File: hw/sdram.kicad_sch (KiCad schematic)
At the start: 23 parts, among them U1002 T20Q144xx, U1004 NDS36PT5-16ET

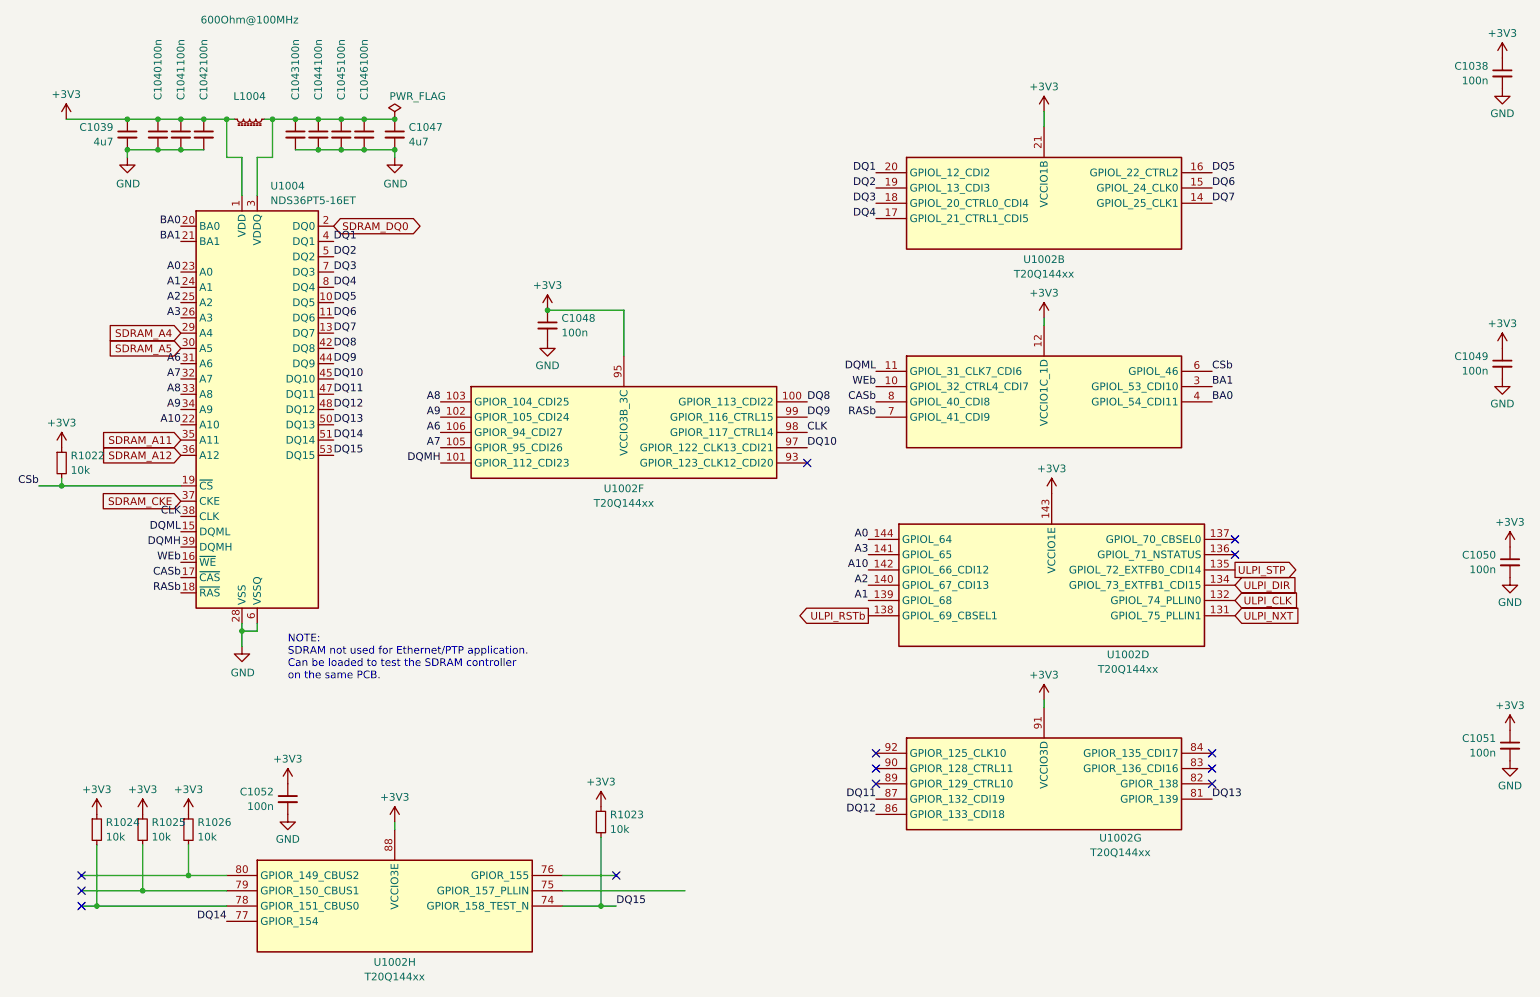
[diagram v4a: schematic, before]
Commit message: layout almost complete with UPLI on the RHS => NO CLOCK INPUT
Have to rework and move the usb transceiver to the left...
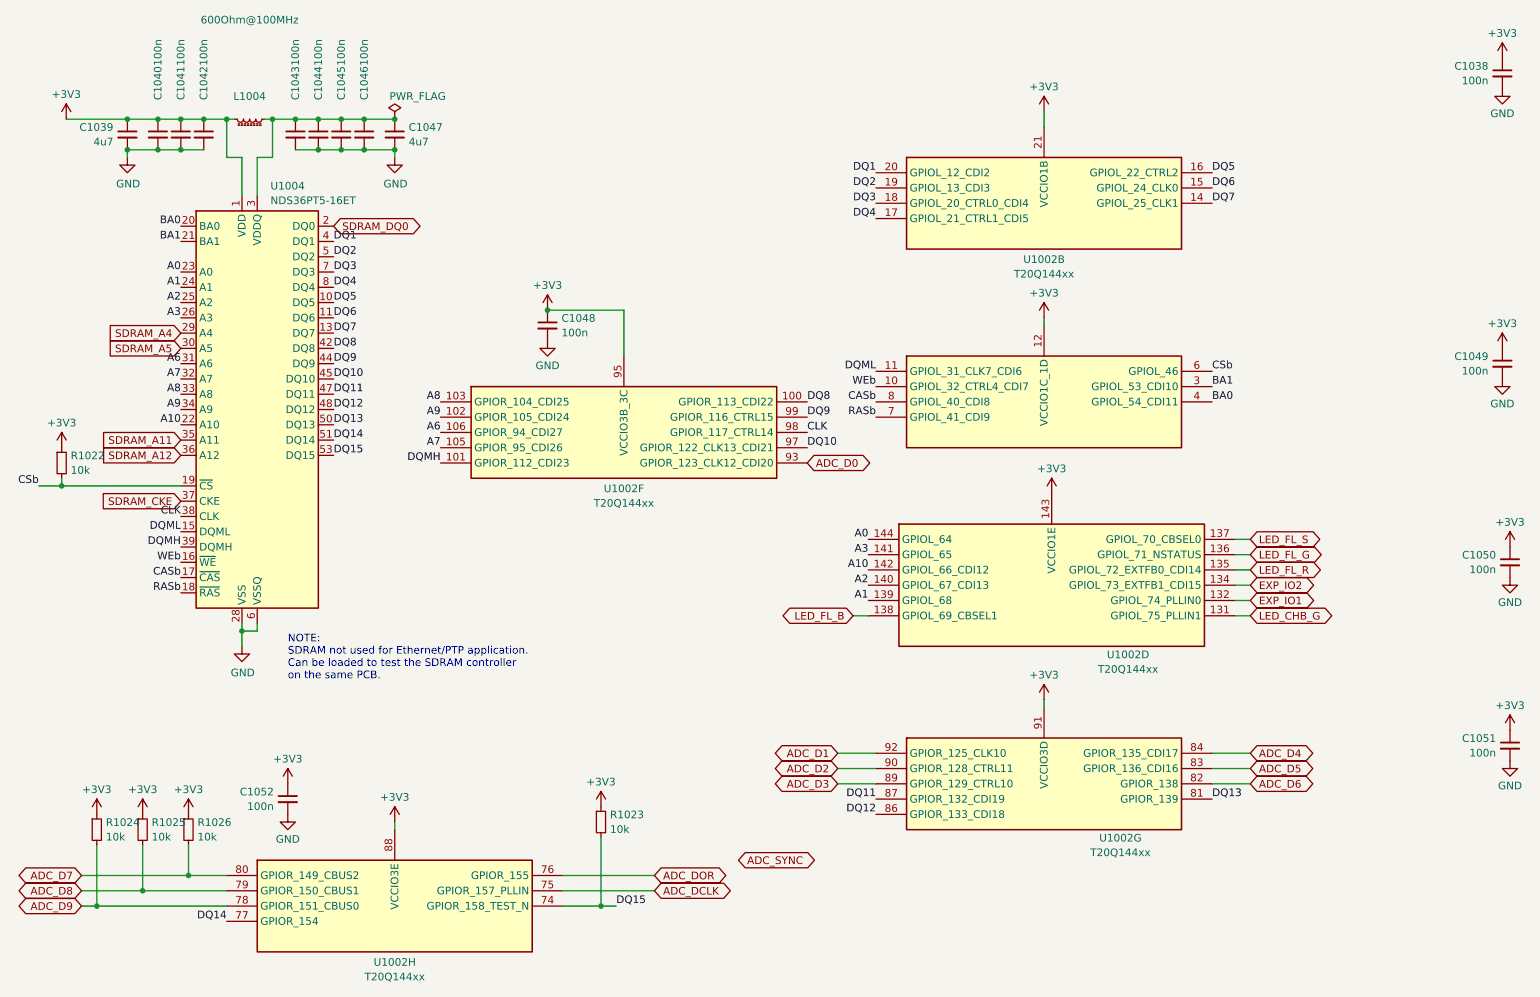
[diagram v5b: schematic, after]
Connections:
- net ADC_D7: now reaches R1026.2, U1002.80 (GPIOR_149_CBUS2)
- net ADC_D0: now reaches U1002.93 (GPIOR_123_CLK12_CDI20)
- net ADC_D9: now reaches R1024.2, U1002.78 (GPIOR_151_CBUS0)
- net ADC_DCLK: now reaches U1002.75 (GPIOR_157_PLLIN)
- net ADC_DOR: now reaches U1002.76 (GPIOR_155)
- net ADC_D8: now reaches R1025.2, U1002.79 (GPIOR_150_CBUS1)
- net LED_FL_G: now reaches U1002.136 (GPIOL_71_NSTATUS)
- net LED_FL_S: now reaches U1002.137 (GPIOL_70_CBSEL0)
- net ADC_D6: now reaches U1002.82 (GPIOR_138)
- net ADC_D5: now reaches U1002.83 (GPIOR_136_CDI16)
- net ADC_D4: now reaches U1002.84 (GPIOR_135_CDI17)
- net ADC_D3: now reaches U1002.89 (GPIOR_129_CTRL10)
- net ADC_D2: now reaches U1002.90 (GPIOR_128_CTRL11)
- net ADC_D1: now reaches U1002.92 (GPIOR_125_CLK10)
- net ULPI_CLK renamed EXP_IO1
- net ULPI_DIR renamed EXP_IO2
- net ULPI_NXT renamed LED_CHB_G
- net ULPI_RSTb renamed LED_FL_B
- net ULPI_STP renamed LED_FL_R
- no-connect marks 13 -> 0

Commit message: finalizing...
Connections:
- net LED_FL_B is gone; now on net A1: U1002.138 (GPIOL_69_CBSEL1)
- net A1: no longer U1002.139 (GPIOL_68)
- net SDRAM_CKE: now also U1002.139 (GPIOL_68)
- net EXP_IO1 renamed ULPI_CLK
- net EXP_IO2 renamed I2C_SCL_3V3
- net LED_CHB_G renamed ULPI_NXT
- net LED_FL_G renamed ULPI_STP
- net LED_FL_R renamed ULPI_DIR
- net LED_FL_S renamed ULPI_RSTb
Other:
- note removed: "NOTE: SDRAM not used for Ethernet/PTP application. Can be loaded to test the SDRAM controller on the same PCB."
- moved on the sheet: R1022

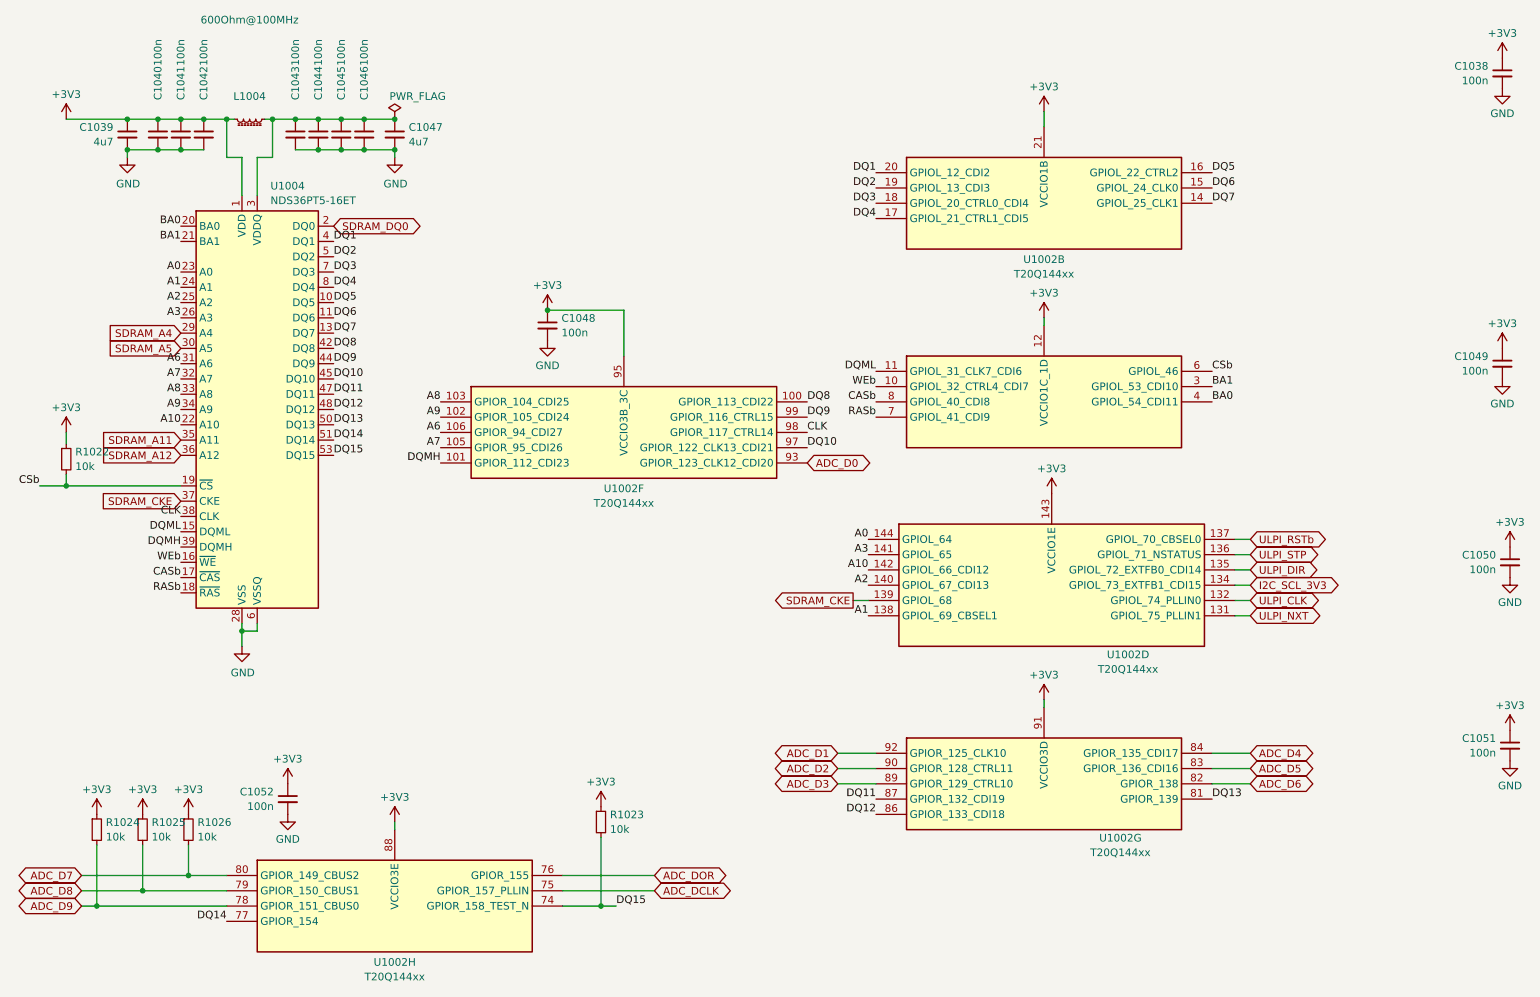
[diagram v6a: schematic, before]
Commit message: renumbered references on trion sub-sheets
Had used numbers > 1000 when merging designs
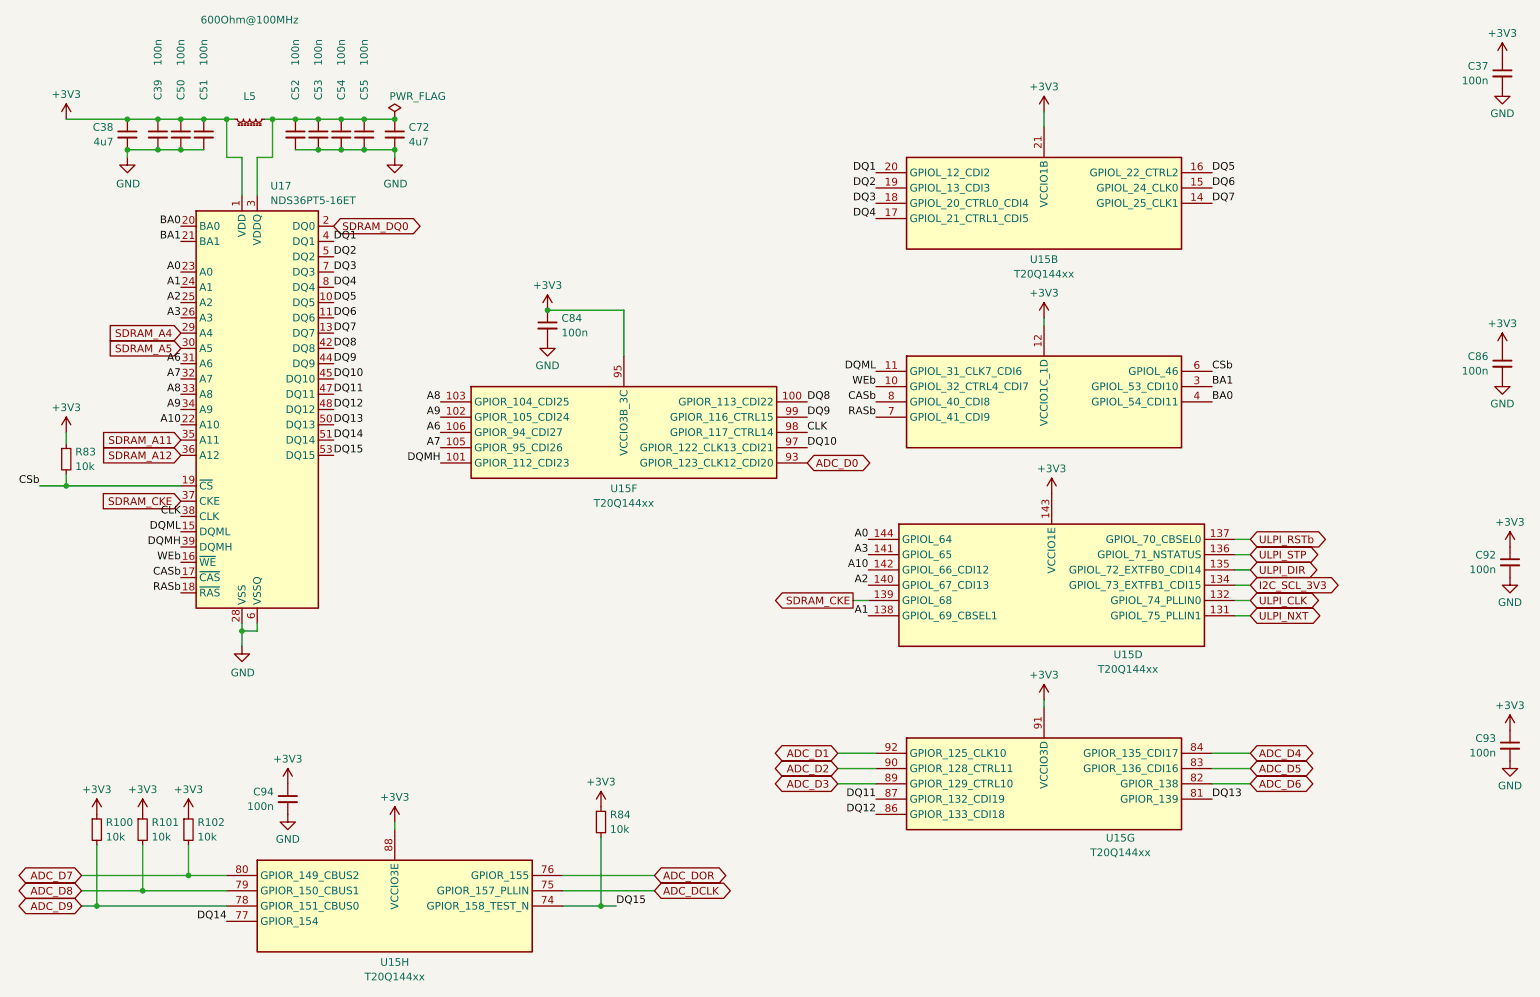
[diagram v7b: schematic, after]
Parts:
- renumbered C1038 to C37, C1039 to C38, C1040 to C39, C1041 to C50, C1042 to C51, C1043 to C52, C1044 to C53, C1045 to C54, C1046 to C55, C1047 to C72, C1048 to C84, C1049 to C86, C1050 to C92, C1051 to C93, C1052 to C94, L1004 to L5, R1024 to R100, R1025 to R101, R1026 to R102, R1022 to R83, R1023 to R84, U1002 to U15, U1004 to U17

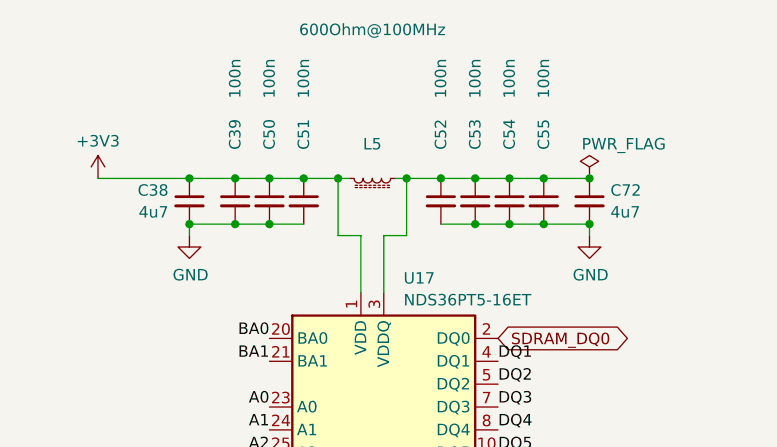
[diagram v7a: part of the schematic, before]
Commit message: consolidated ferrite beads (use same everywhere)
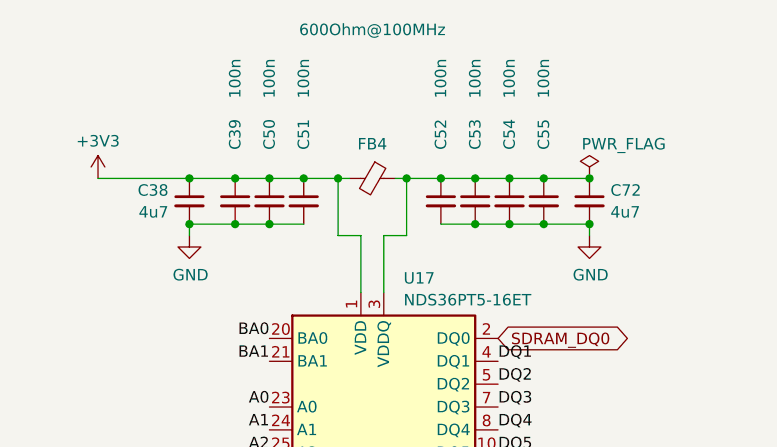
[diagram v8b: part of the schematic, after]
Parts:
- FB4: renamed from L5; symbol Device:L_Ferrite_Small -> Device:FerriteBead_Small
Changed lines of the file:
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@@
     )
   )
-  (symbol (lib_id "Device:L_Ferrite_Small") (at 55.88 40.64 270) (unit 1)
+  (symbol (lib_id "Device:FerriteBead_Small") (at 55.88 40.64 270) (unit 1)
     (in_bom yes) (on_board yes) (dnp no)
-    (property "Reference" "L5" (at 55.88 36.83 90)
+    (property "Reference" "FB4" (at 55.88 36.83 90)
       (effects (font (size 1.27 1.27)))
     )
@@
       (effects (font (size 1.27 1.27)))
     )
-    (property "Footprint" "Inductor_SMD:L_0603_1608Metric" (at 55.88 40.64 0)
+    (property "Footprint" "Inductor_SMD:L_0603_1608Metric" (at 55.88 38.862 90)
       (effects (font (size 1.27 1.27)) hide)
     )
@@
       (project "usbadc"
         (path "/7c8a1f8d-8834-4c9b-aaae-1f231e9b09a1/d9cd2a48-41b0-4b01-a978-0843576735ad/1b523d49-ff11-41b3-8609-dd0dd8346ed0"
-          (reference "L5") (unit 1)
+          (reference "FB4") (unit 1)
         )
       )
